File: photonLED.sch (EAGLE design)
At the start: 15 parts, among them T1 MJD32C, T2 MJD32C, T3 MJD32C, T4 MJD32C

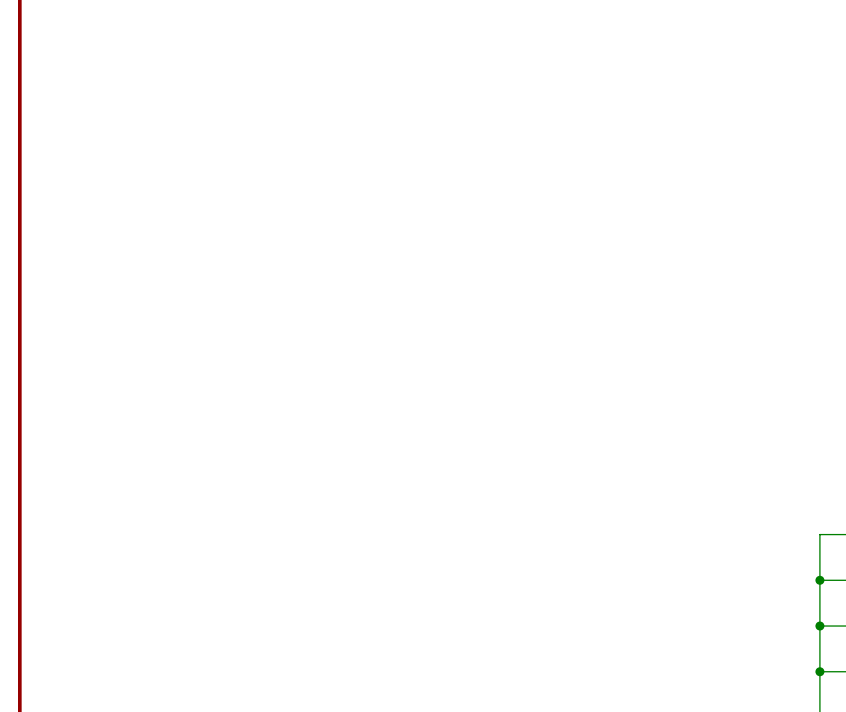
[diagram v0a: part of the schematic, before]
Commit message: added voltage regulator, DC terminals, all on one side.
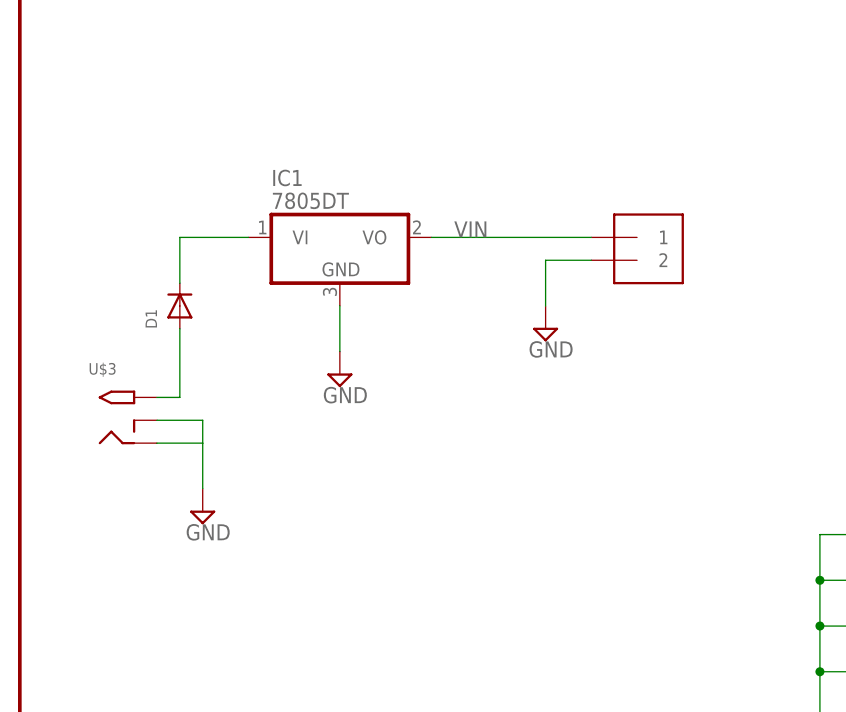
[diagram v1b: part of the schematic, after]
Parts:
- added D1: (no value), adafruit:DIODESOD-123
- added IC1: 7805DT, adafruit:7805DT
- added J1: 3.5MM Screw Term, adafruit:1X2-3.5MM
- added U$3: 2.1MMJACKSMT, adafruit:2.1MMJACKSMT
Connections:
- new net N$10: D1.C, IC1.VI
- new net N$9: D1.A, U$3.TIP
- net GND: now also IC1.GND, J1.2, U$3.RING, U$3.RING_SW
- net VIN: now also IC1.VO, J1.1
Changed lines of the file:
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@@
 <setting verticaltext="up"/>
 </settings>
-<grid distance="0.1" unitdist="inch" unit="inch" style="lines" multiple="1" display="yes" altdistance="0.01" altunitdist="inch" altunit="inch"/>
+<grid distance="0.1" unitdist="inch" unit="inch" style="lines" multiple="1" display="no" altdistance="0.01" altunitdist="inch" altunit="inch"/>
 <layers>
-<layer number="1" name="Top" color="4" fill="1" visible="yes" active="no"/>
-<layer number="2" name="Route2" color="1" fill="3" visible="yes" active="no"/>
-<layer number="3" name="Route3" color="4" fill="3" visible="yes" active="no"/>
-<layer number="14" name="Route14" color="1" fill="6" visible="yes" active="no"/>
-<layer number="15" name="Route15" color="4" fill="6" visible="yes" active="no"/>
-<layer number="16" name="Bottom" color="1" fill="1" visible="yes" active="no"/>
-<layer number="17" name="Pads" color="2" fill="1" visible="yes" active="no"/>
-<layer number="18" name="Vias" color="2" fill="1" visible="yes" active="no"/>
-<layer number="19" name="Unrouted" color="6" fill="1" visible="yes" active="no"/>
-<layer number="20" name="Dimension" color="15" fill="1" visible="yes" active="no"/>
-<layer number="21" name="tPlace" color="7" fill="1" visible="yes" active="no"/>
-<layer number="22" name="bPlace" color="7" fill="1" visible="yes" active="no"/>
-<layer number="23" name="tOrigins" color="15" fill="1" visible="yes" active="no"/>
-<layer number="24" name="bOrigins" color="15" fill="1" visible="yes" active="no"/>
-<layer number="25" name="tNames" color="7" fill="1" visible="yes" active="no"/>
-<layer number="26" name="bNames" color="7" fill="1" visible="yes" active="no"/>
-<layer number="27" name="tValues" color="7" fill="1" visible="yes" active="no"/>
-<layer number="28" name="bValues" color="7" fill="1" visible="yes" active="no"/>
+<layer number="1" name="Top" color="4" fill="1" visible="no" active="no"/>
+<layer number="2" name="Route2" color="1" fill="3" visible="no" active="no"/>
+<layer number="3" name="Route3" color="4" fill="3" visible="no" active="no"/>
+<layer number="14" name="Route14" color="1" fill="6" visible="no" active="no"/>
+<layer number="15" name="Route15" color="4" fill="6" visible="no" active="no"/>
+<layer number="16" name="Bottom" color="1" fill="1" visible="no" active="no"/>
+<layer number="17" name="Pads" color="2" fill="1" visible="no" active="no"/>
+<layer number="18" name="Vias" color="2" fill="1" visible="no" active="no"/>
+<layer number="19" name="Unrouted" color="6" fill="1" visible="no" active="no"/>
+<layer number="20" name="Dimension" color="15" fill="1" visible="no" active="no"/>
+<layer number="21" name="tPlace" color="7" fill="1" visible="no" active="no"/>
+<layer number="22" name="bPlace" color="7" fill="1" visible="no" active="no"/>
+<layer number="23" name="tOrigins" color="15" fill="1" visible="no" active="no"/>
+<layer number="24" name="bOrigins" color="15" fill="1" visible="no" active="no"/>
+<layer number="25" name="tNames" color="7" fill="1" visible="no" active="no"/>
+<layer number="26" name="bNames" color="7" fill="1" visible="no" active="no"/>
+<layer number="27" name="tValues" color="7" fill="1" visible="no" active="no"/>
+<layer number="28" name="bValues" color="7" fill="1" visible="no" active="no"/>
 <layer number="29" name="tStop" color="7" fill="3" visible="no" active="no"/>
 <layer number="30" name="bStop" color="7" fill="6" visible="no" active="no"/>
@@
 <layer number="35" name="tGlue" color="7" fill="4" visible="no" active="no"/>
 <layer number="36" name="bGlue" color="7" fill="5" visible="no" active="no"/>
-<layer number="37" name="tTest" color="7" fill="1" visible="yes" active="no"/>
-<layer number="38" name="bTest" color="7" fill="1" visible="yes" active="no"/>
+<layer number="37" name="tTest" color="7" fill="1" visible="no" active="no"/>
+<layer number="38" name="bTest" color="7" fill="1" visible="no" active="no"/>
 <layer number="39" name="tKeepout" color="4" fill="11" visible="no" active="no"/>
 <layer number="40" name="bKeepout" color="1" fill="11" visible="no" active="no"/>
@@
 <layer number="44" name="Drills" color="7" fill="1" visible="no" active="no"/>
 <layer number="45" name="Holes" color="7" fill="1" visible="no" active="no"/>
-<layer number="46" name="Milling" color="3" fill="1" visible="yes" active="no"/>
-<layer number="47" name="Measures" color="7" fill="1" visible="yes" active="no"/>
-<layer number="48" name="Document" color="7" fill="1" visible="yes" active="no"/>
-<layer number="49" name="Reference" color="7" fill="1" visible="yes" active="no"/>
-<layer number="50" name="dxf" color="7" fill="1" visible="yes" active="no"/>
-<layer number="51" name="tDocu" color="7" fill="1" visible="yes" active="no"/>
-<layer number="52" name="bDocu" color="7" fill="1" visible="yes" active="no"/>
-<layer number="53" name="tGND_GNDA" color="7" fill="9" visible="yes" active="no"/>
-<layer number="54" name="bGND_GNDA" color="1" fill="9" visible="yes" active="no"/>
-<layer number="56" name="wert" color="7" fill="1" visible="yes" active="no"/>
-<layer number="57" name="tCAD" color="7" fill="1" visible="yes" active="no"/>
-<layer number="59" name="tCarbon" color="7" fill="1" visible="yes" active="no"/>
-<layer number="60" name="bCarbon" color="7" fill="1" visible="yes" active="no"/>
+<layer number="46" name="Milling" color="3" fill="1" visible="no" active="no"/>
+<layer number="47" name="Measures" color="7" fill="1" visible="no" active="no"/>
+<layer number="48" name="Document" color="7" fill="1" visible="no" active="no"/>
+<layer number="49" name="Reference" color="7" fill="1" visible="no" active="no"/>
+<layer number="50" name="dxf" color="7" fill="1" visible="no" active="no"/>
+<layer number="51" name="tDocu" color="7" fill="1" visible="no" active="no"/>
+<layer number="52" name="bDocu" color="7" fill="1" visible="no" active="no"/>
+<layer number="53" name="tGND_GNDA" color="7" fill="9" visible="no" active="no"/>
+<layer number="54" name="bGND_GNDA" color="1" fill="9" visible="no" active="no"/>
+<layer number="56" name="wert" color="7" fill="1" visible="no" active="no"/>
+<layer number="57" name="tCAD" color="7" fill="1" visible="no" active="no"/>
+<layer number="59" name="tCarbon" color="7" fill="1" visible="no" active="no"/>
+<layer number="60" name="bCarbon" color="7" fill="1" visible="no" active="no"/>
 <layer number="90" name="Modules" color="5" fill="1" visible="yes" active="yes"/>
 <layer number="91" name="Nets" color="2" fill="1" visible="yes" active="yes"/>
@@
 <part name="SUPPLY3" library="supply2" deviceset="GND" device=""/>
 <part name="U$2" library="emily" deviceset="MC-E" device=""/>
+<part name="IC1" library="adafruit" deviceset="78*" device="DT" technology="05"/>
+<part name="SUPPLY4" library="supply2" deviceset="GND" device=""/>
+<part name="U$3" library="adafruit" deviceset="2.1MMJACK" device="SMT"/>
+<part name="SUPPLY5" library="supply2" deviceset="GND" device=""/>
+<part name="D1" library="adafruit" deviceset="DIODE" device="SOD-123"/>
+<part name="J1" library="adafruit" deviceset="1X2" device="-3.5MM" value="3.5MM Screw Term"/>
+<part name="SUPPLY6" library="supply2" deviceset="GND" device=""/>
 </parts>
 <sheets>
@@
 <instance part="SUPPLY3" gate="GND" x="15.24" y="86.36"/>
 <instance part="U$2" gate="G$1" x="99.06" y="104.14"/>
+<instance part="IC1" gate="A1" x="35.56" y="154.94"/>
+<instance part="SUPPLY4" gate="GND" x="35.56" y="139.7"/>
+<instance part="U$3" gate="G$1" x="10.16" y="134.62"/>
+<instance part="SUPPLY5" gate="GND" x="20.32" y="124.46"/>
+<instance part="D1" gate="G$1" x="17.78" y="147.32" rot="R90"/>
+<instance part="J1" gate="G$1" x="68.58" y="152.4"/>
+<instance part="SUPPLY6" gate="GND" x="58.42" y="144.78"/>
 </instances>
 <busses>
@@
 <wire x1="30.48" y1="88.9" x2="15.24" y2="88.9" width="0.1524" layer="91"/>
 </segment>
+<segment>
+<pinref part="SUPPLY4" gate="GND" pin="GND"/>
+<pinref part="IC1" gate="A1" pin="GND"/>
+<wire x1="35.56" y1="142.24" x2="35.56" y2="147.32" width="0.1524" layer="91"/>
+</segment>
+<segment>
+<pinref part="J1" gate="G$1" pin="2"/>
+<pinref part="SUPPLY6" gate="GND" pin="GND"/>
+<wire x1="63.5" y1="152.4" x2="58.42" y2="152.4" width="0.1524" layer="91"/>
+<wire x1="58.42" y1="152.4" x2="58.42" y2="147.32" width="0.1524" layer="91"/>
+</segment>
+<segment>
+<pinref part="U$3" gate="G$1" pin="RING"/>
+<wire x1="15.24" y1="132.08" x2="20.32" y2="132.08" width="0.1524" layer="91"/>
+<pinref part="U$3" gate="G$1" pin="RING_SW"/>
+<wire x1="20.32" y1="132.08" x2="20.32" y2="134.62" width="0.1524" layer="91"/>
+<wire x1="20.32" y1="134.62" x2="15.24" y2="134.62" width="0.1524" layer="91"/>
+<pinref part="SUPPLY5" gate="GND" pin="GND"/>
+<wire x1="20.32" y1="127" x2="20.32" y2="132.08" width="0.1524" layer="91"/>
+</segment>
 </net>
 <net name="VIN" class="0">
@@
 <label x="218.44" y="160.02" size="1.778" layer="95"/>
 </segment>
+<segment>
+<pinref part="IC1" gate="A1" pin="VO"/>
+<label x="48.26" y="154.94" size="1.778" layer="95"/>
+<pinref part="J1" gate="G$1" pin="1"/>
+<wire x1="63.5" y1="154.94" x2="45.72" y2="154.94" width="0.1524" layer="91"/>
+</segment>
 </net>
 <net name="N$11" class="0">
@@
 </segment>
 </net>
+<net name="N$9" class="0">
+<segment>
+<pinref part="U$3" gate="G$1" pin="TIP"/>
+<pinref part="D1" gate="G$1" pin="A"/>
+<wire x1="15.24" y1="137.16" x2="17.78" y2="137.16" width="0.1524" layer="91"/>
+<wire x1="17.78" y1="137.16" x2="17.78" y2="144.78" width="0.1524" layer="91"/>
+</segment>
+</net>
+<net name="N$10" class="0">
+<segment>
+<pinref part="D1" gate="G$1" pin="C"/>
+<wire x1="17.78" y1="149.86" x2="17.78" y2="154.94" width="0.1524" layer="91"/>
+<pinref part="IC1" gate="A1" pin="VI"/>
+<wire x1="17.78" y1="154.94" x2="25.4" y2="154.94" width="0.1524" layer="91"/>
+</segment>
+</net>

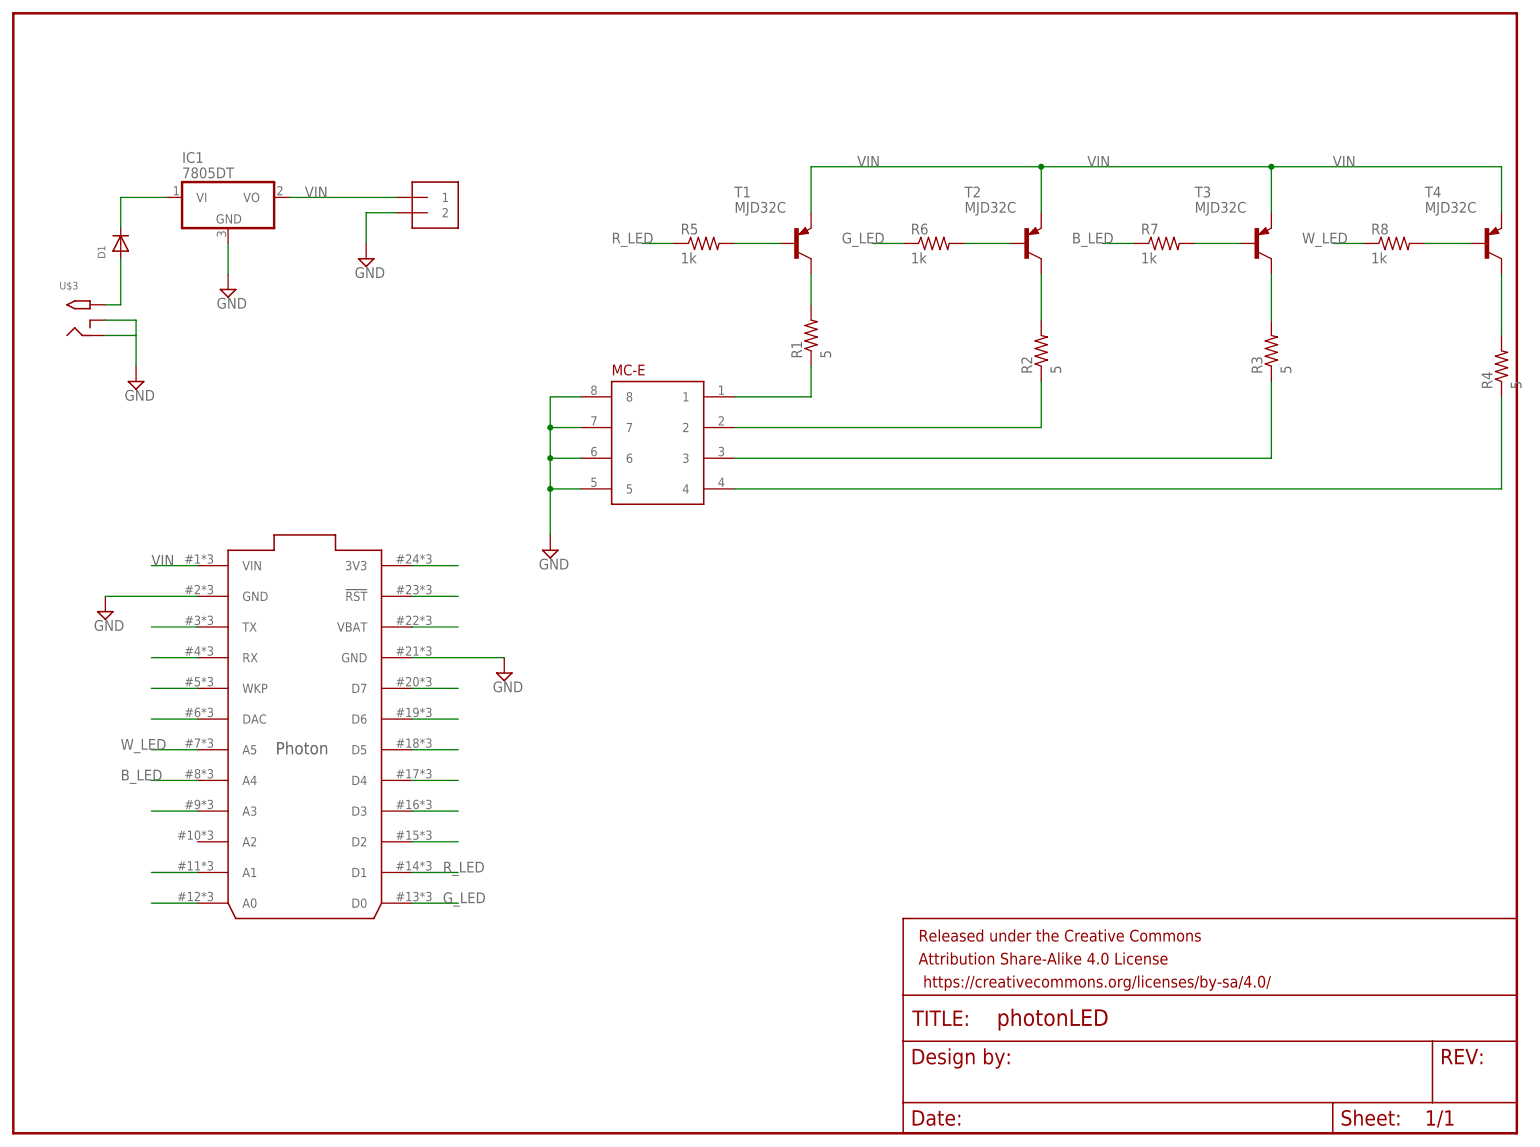
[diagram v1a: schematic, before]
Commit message: added color sensor, mounting holes, ground planes, etc.
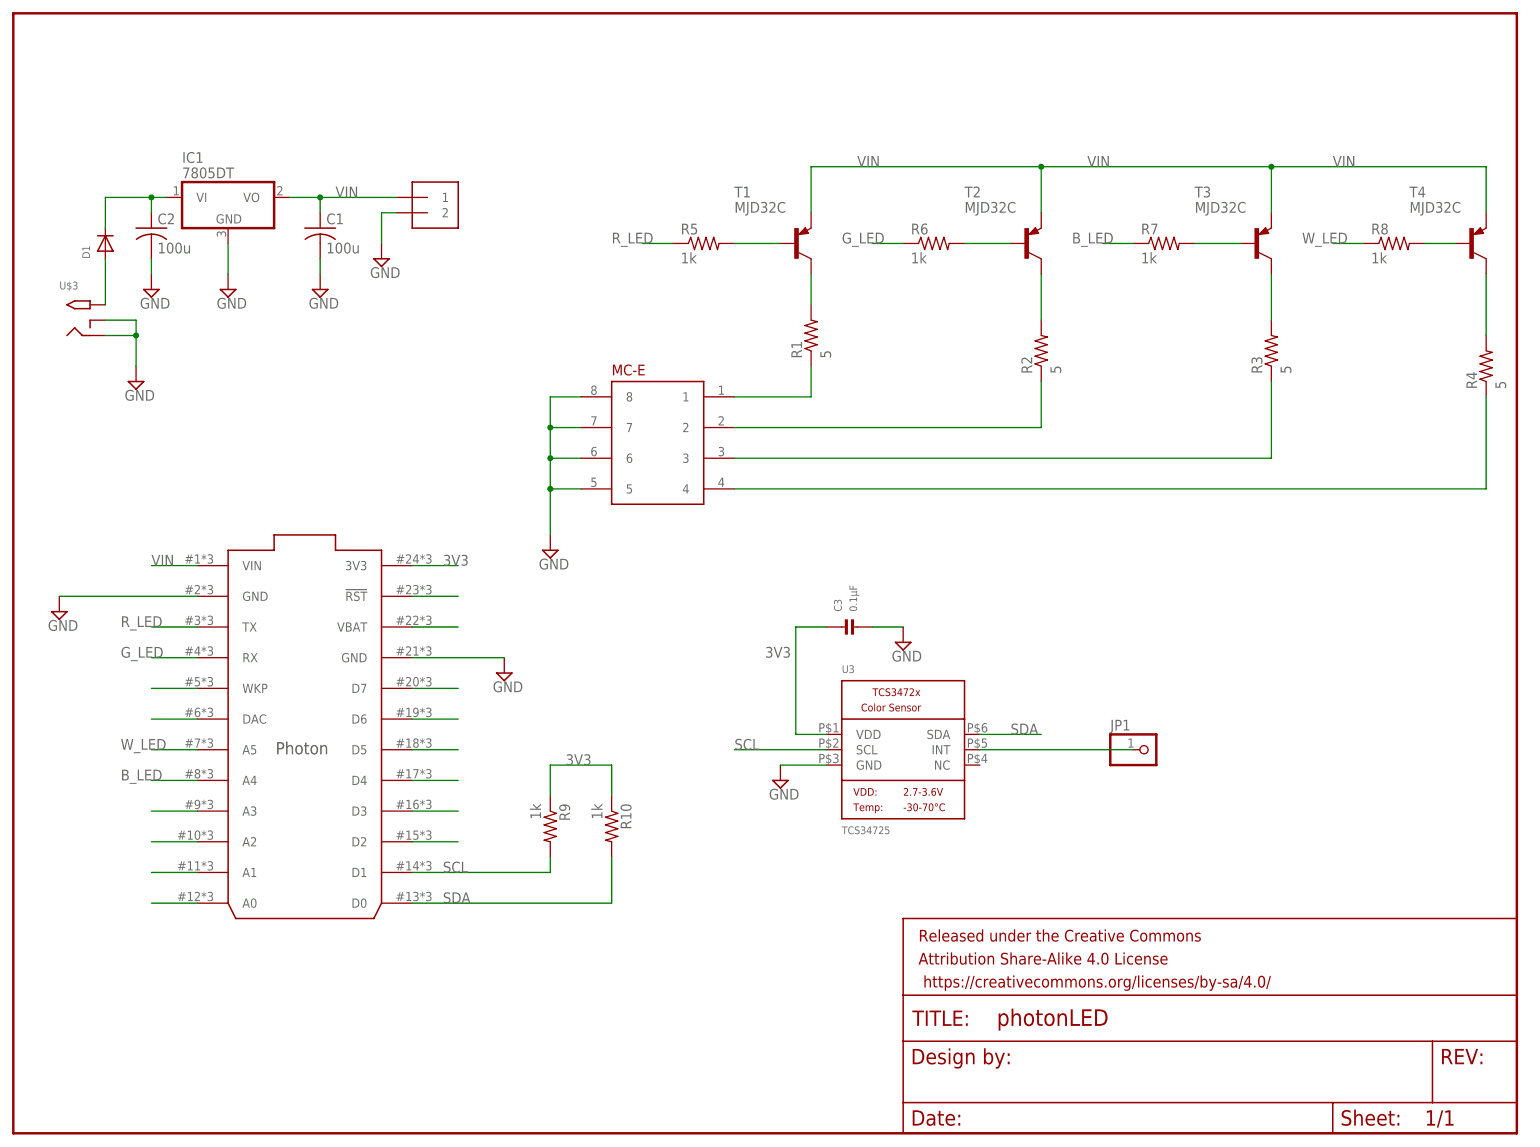
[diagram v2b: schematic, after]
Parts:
- added C1, C2: 100u, adafruit:C-USC0805
- added C3: 0.1µF, microbuilder:CAP_CERAMIC_0805
- added JP1: (no value), adafruit:PINHD-1X1
- added R10, R9: 1k, adafruit:R-US_R0805
- added U3: TCS34725, microbuilder:LIGHT_TCS3472
- U$1: value Photon -> (none)
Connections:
- removed net N$21: U$1.3V3
- new net 3V3: C3.P$1, R10.1, R9.1, U$1.3V3, U3.VDD
- new net SCL: R9.2, U$1.D1, U3.SCL
- new net SDA: R10.2, U$1.D0, U3.SDA
- net GND: now also C1.2, C2.2, C3.P$2, U3.GND
- net G_LED: now also U$1.RX; no longer U$1.D0
- net N$10: now also C2.1
- net N$11: now also JP1.1, U3.INT; no longer U$1.TX
- net N$12: now also U$1.A2; no longer U$1.RX
- net R_LED: now also U$1.TX; no longer U$1.D1
- net VIN: now also C1.1
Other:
- moved on the sheet: D1, R4, T4
